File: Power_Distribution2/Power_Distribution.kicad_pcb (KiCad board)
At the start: 2 copper layers, 84.5 x 59 mm, 23 parts, among them J1 Out1, J2 Out2, J3 Out3, J4 Out4, J5 Out5, J6 Out6, J7 Out7, J8 Out8

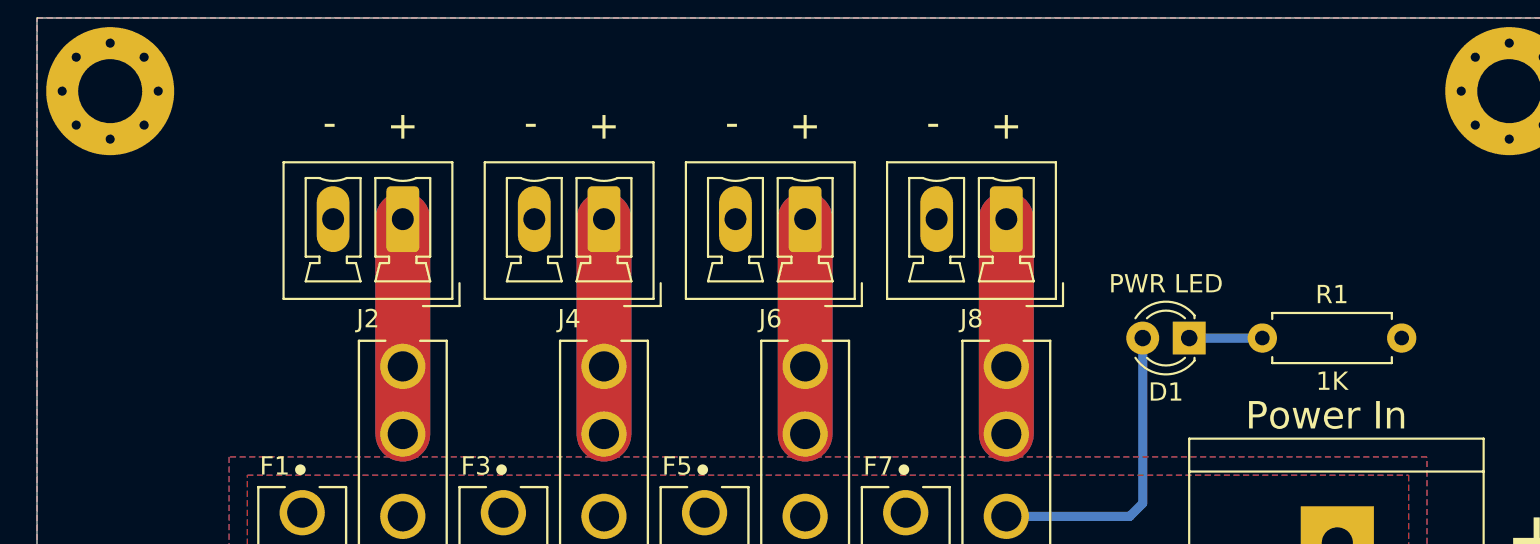
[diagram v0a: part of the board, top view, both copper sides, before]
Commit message: added power distros
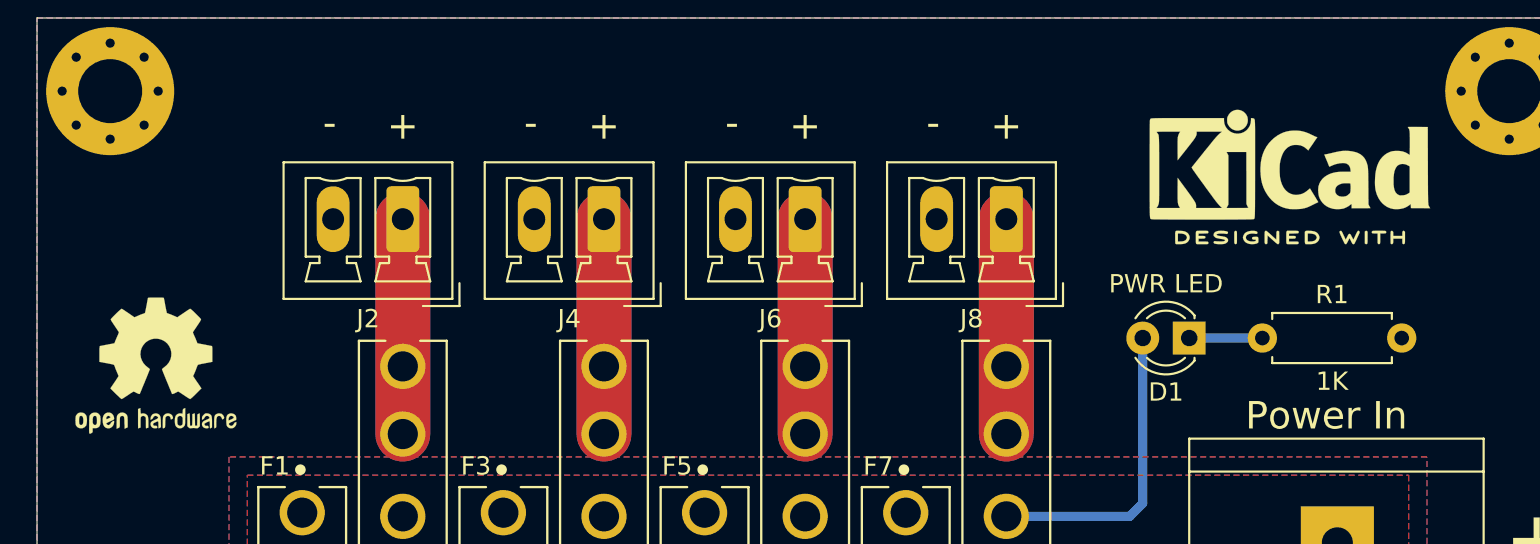
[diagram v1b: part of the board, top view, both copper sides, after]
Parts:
- added REF**: OSHW-Logo2_9.8x8mm_SilkScreen, Symbol:OSHW-Logo2_9.8x8mm_SilkScreen, F.Cu at (94.0, 91.0)
- added REF**: KiCad-Logo2_6mm_SilkScreen, Symbol:KiCad-Logo2_6mm_SilkScreen, F.Cu at (156.0, 80.0)
